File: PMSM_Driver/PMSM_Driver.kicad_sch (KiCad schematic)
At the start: 276 parts, among them J1 2606-1101, J10 AFBR-2624Z, J11 AFBR-2624Z, J12 AFBR-2624Z, J13 AFBR-2624Z, J14 AFBR-2624Z, J15 AFBR-2624Z, J16 AFBR-2624Z, J17 2606-1101, J18 2606-1101, J2 AFBR-2624Z, J3 1714971, J4 1714971, J5 1827907, J6 AFBR-2624Z, J7 AFBR-2624Z, J8 AFBR-2624Z, J9 AFBR-2624Z, Q1 BC846, Q10 BC846, Q11 RGCL60TK60, Q12 RGCL60TK60, Q13 RGCL60TK60, Q14 RGCL60TK60, Q15 BC846, Q16 RGCL60TK60, Q17 RGCL60TK60, Q18 RGCL60TK60, Q19 RGCL60TK60, Q2 BC846, Q20 BC846, Q21 BC846, Q22 BC846, Q23 BC846, Q24 BC846, Q3 BC846, Q4 BC846, Q5 RGCL60TK60, Q6 RGCL60TK60, Q7 RGCL60TK60, Q8 RGCL60TK60, Q9 BC846, U1 74LVC1G04, U10 HCPL-3120, U11 HCPL-3120, U12 HCPL-3120, U13 74LVC1G04, U14 74LVC1G04, U15 74LVC1G04, U16 MGJ2D051515SC, U17 MGJ2D051515SC, U18 MGJ2D051515SC, U19 HCPL-3120, U2 MGJ2D051515SC, U20 HCPL-3120, U21 HCPL-3120, U22 74LVC1G04, U23 74LVC1G04, U24 74LVC1G04, U25 MGJ2D051515SC, U26 MGJ2D051515SC, U27 MGJ2D051515SC, U28 HCPL-3120, U29 HCPL-3120, U3 HCPL-3120, U30 HCPL-3120, U31 74LVC1G04, U32 74LVC1G04, U33 MGJ2D051515SC, U34 MGJ2D051515SC, U35 HCPL-3120, U36 HCPL-3120, U37 VS-E5TH3006S2L-M3, U38 VS-E5TH3006S2L-M3, U39 VS-E5TH3006S2L-M3, U4 74LVC1G04, U40 VS-E5TH3006S2L-M3, U41 VS-E5TH3006S2L-M3, U42 VS-E5TH3006S2L-M3, U43 VS-E5TH3006S2L-M3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

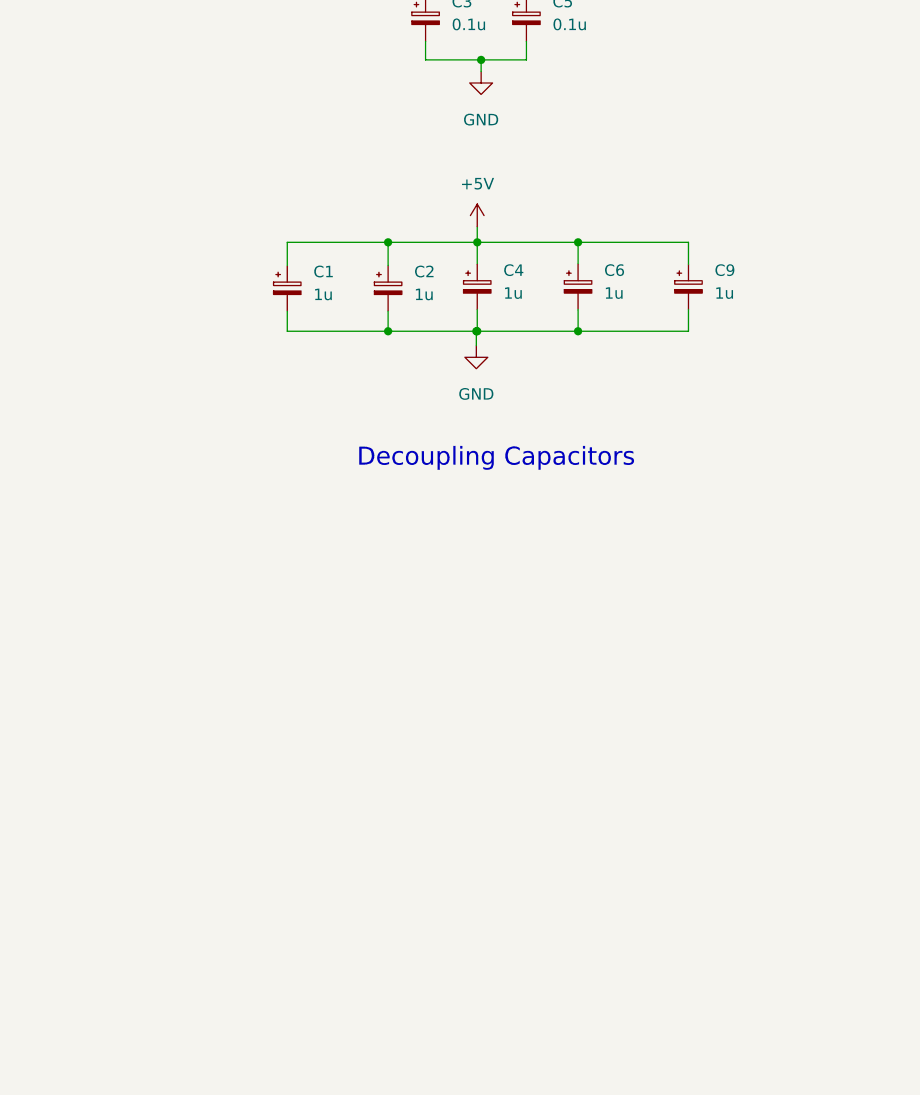
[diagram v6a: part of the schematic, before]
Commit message: filled zone completed, Fiber-Optic and size of resistors need to be replaced
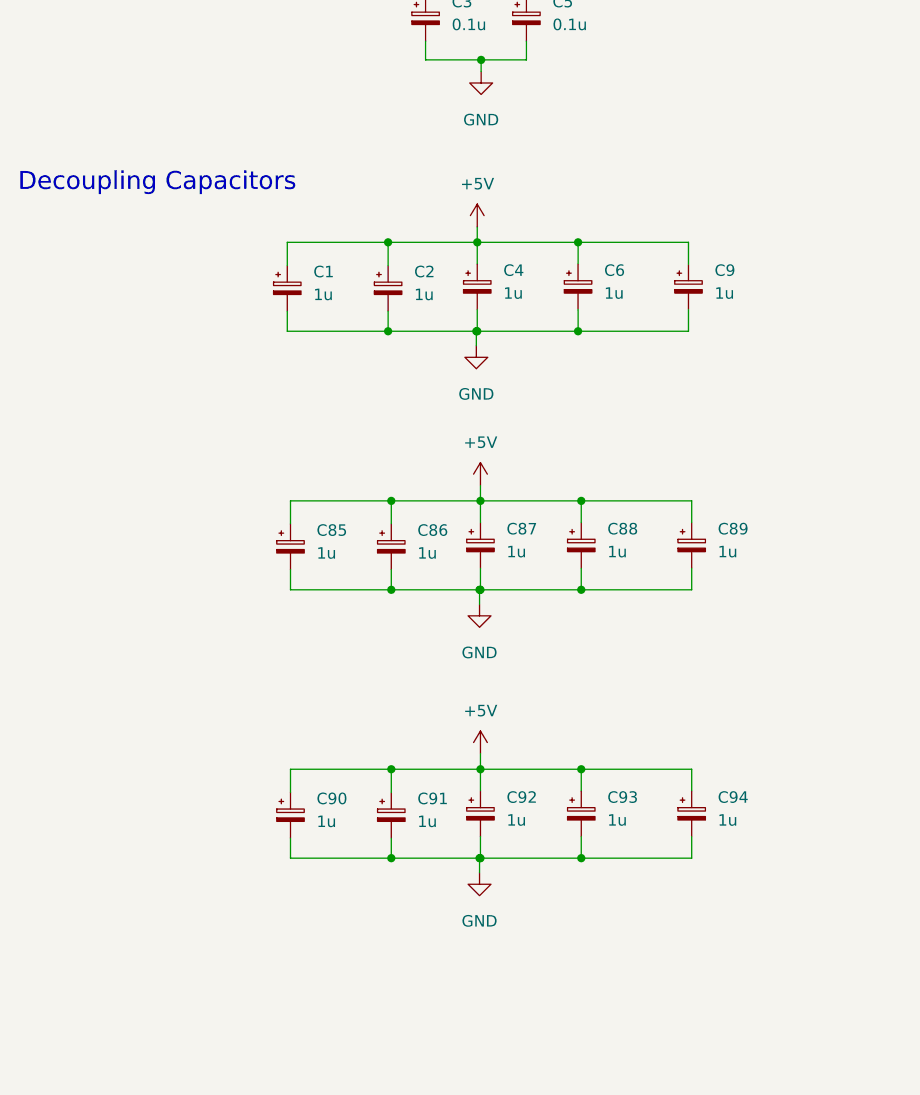
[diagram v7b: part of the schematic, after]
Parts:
- added C85, C86, C87, C88, C89, C90, C91, C92, C93, C94: 1u, Capacitor_SMD:C_0402_1005Metric, symbol Device:C_Polarized_Small
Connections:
- net +5V: now also C85.1, C86.1, C87.1, C88.1, C89.1, C90.1, C91.1, C92.1, C93.1, C94.1
- net GND: now also C85.2, C86.2, C87.2, C88.2, C89.2, C90.2, C91.2, C92.2, C93.2, C94.2

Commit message: filled zone completed, some SMD components need to be re-selected
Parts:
- removed C3, C5: 0.1u, Capacitor_SMD:C_0402_1005Metric, symbol Device:C_Polarized_Small
- removed J10, J11, J12, J13, J14, J15, J16, J2, J6, J7, J8, J9: AFBR-2624Z, OptoDevice:Broadcom_AFBR-16xxZ_Horizontal, symbol Fiber_Optic:AFBR-2624Z
- added C6, C9: 0.1u, Capacitor_SMD:C_1206_3216Metric, symbol Device:C_Polarized_Small
- added J10, J11, J12, J13, J14, J15, J16, J2, J6, J7, J8, J9: HFBR-2521Z, OptoDevice:Broadcom_AFBR-16xxZ_Horizontal, symbol FYP_Components:HFBR-2521Z
- C1, C2, C85, C86, C87, C88, C89: value 1u -> 0.1u; footprint Capacitor_SMD:C_0402_1005Metric -> Capacitor_SMD:C_1206_3216Metric
- C10, C11, C12, C13, C16, C17, C18, C19, C20, C21, C22, C23, C24, C25, C26, C27, C28, C29, C30, C31, C32, C33, C34, C35, C36, C37, C38, C39, C40, C41, C42, C43, C44, C45, C46, C47, C48, C49, C50, C51, C52, C53, C54, C55, C56, C57, C58, C59, C60, C61, C62, C63, C64, C65, C66, C67, C68, C69, C7, C70, C71, C72, C73, C74, C75, C76, C77, C78, C79, C8, C80, C81, C90, C91, C92, C93, C94: footprint Capacitor_SMD:C_0402_1005Metric -> Capacitor_SMD:C_1206_3216Metric
- C3: renamed from C4; value 1u -> 0.1u; footprint Capacitor_SMD:C_0402_1005Metric -> Capacitor_SMD:C_1206_3216Metric
- C4: renamed from C6; value 1u -> 0.1u; footprint Capacitor_SMD:C_0402_1005Metric -> Capacitor_SMD:C_1206_3216Metric
- C5: renamed from C9; value 1u -> 0.1u; footprint Capacitor_SMD:C_0402_1005Metric -> Capacitor_SMD:C_1206_3216Metric
- C82, C83, C84: footprint Capacitor_SMD:C_0603_1608Metric -> Capacitor_SMD:C_1206_3216Metric
- R1, R10, R11, R12, R13, R14, R15, R16, R17, R18, R19, R2, R20, R21, R22, R23, R24, R25, R26, R27, R28, R29, R3, R30, R31, R32, R33, R34, R35, R36, R37, R38, R39, R4, R40, R41, R42, R43, R44, R45, R46, R47, R48, R49, R5, R50, R51, R52, R53, R54, R55, R56, R57, R58, R59, R6, R60, R61, R62, R7, R8, R9: footprint Resistor_SMD:R_0603_1608Metric -> Resistor_SMD:R_1206_3216Metric
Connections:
- net +5V: now also C6.1, C9.1, J10.3 (VCC), J11.3 (VCC), J12.3 (VCC), J13.3 (VCC), J14.3 (VCC), J15.3 (VCC), J16.3 (VCC), J2.3 (VCC), J6.3 (VCC), J7.3 (VCC), J8.3 (VCC), J9.3 (VCC)
- net GND: now also C6.2, C9.2, J10.2 (VEE), J11.2 (VEE), J12.2 (VEE), J13.2 (VEE), J14.2 (VEE), J15.2 (VEE), J16.2 (VEE), J2.2 (VEE), J6.2 (VEE), J7.2 (VEE), J8.2 (VEE), J9.2 (VEE)
- net at U6.2: now also J10.1 (Data_Out), J10.4 (Data_Out)
- net at U1.2: now also J7.1 (Data_Out), J7.4 (Data_Out)
- net at U13.2: now also J9.1 (Data_Out), J9.4 (Data_Out)
- net at U14.2: now also J8.1 (Data_Out), J8.4 (Data_Out)
- net at U31.2: now also J15.1 (Data_Out), J15.4 (Data_Out)
- net at U22.2: now also J12.1 (Data_Out), J12.4 (Data_Out)
- net at U32.2: now also J14.1 (Data_Out), J14.4 (Data_Out)
- net at U15.2: now also J13.1 (Data_Out), J13.4 (Data_Out)
- net at U5.2: now also J6.1 (Data_Out), J6.4 (Data_Out)
- net at U4.2: now also J2.1 (Data_Out), J2.4 (Data_Out)
- net at U23.2: now also J11.1 (Data_Out), J11.4 (Data_Out)
- net at U24.2: now also J16.1 (Data_Out), J16.4 (Data_Out)
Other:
- moved on the sheet: C1, C2, C3, C4, C5, C82, C83, C84, U55, U56, U57, U58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
